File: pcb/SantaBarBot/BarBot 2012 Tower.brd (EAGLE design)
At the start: 53.3 x 73.4 mm, 49 parts, among them J1 AVR_SPI_PRG_62X3_LOCK, J2 POWER_JACKSLT, U1 ATMEGA328P, U2 L298_BRIDGE_DRIVER, U3 742G04DBVR, U5 LMV324IDR, U6 SN75HVD179D

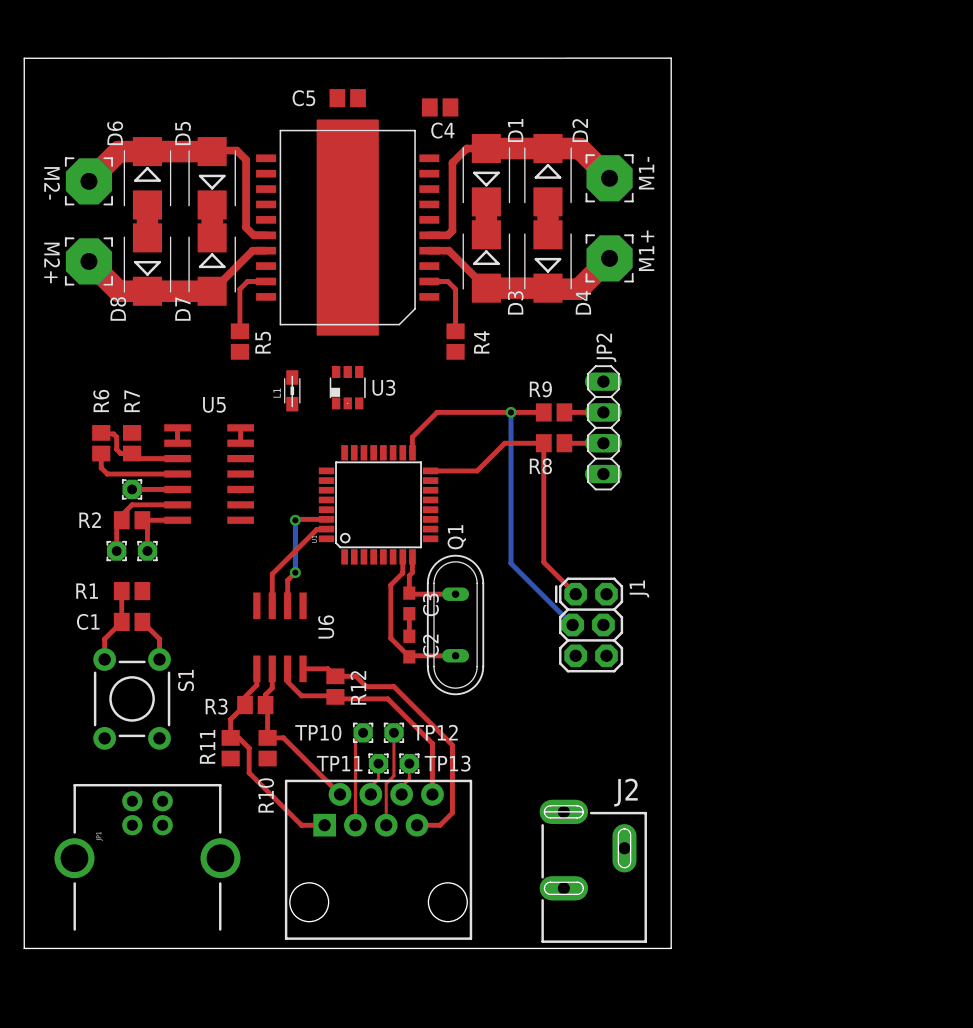
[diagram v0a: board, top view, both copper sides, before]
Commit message: Finished routing PCB, added PDFs of board and schematic to directory, generated netlist, pinlist, and partslist for design
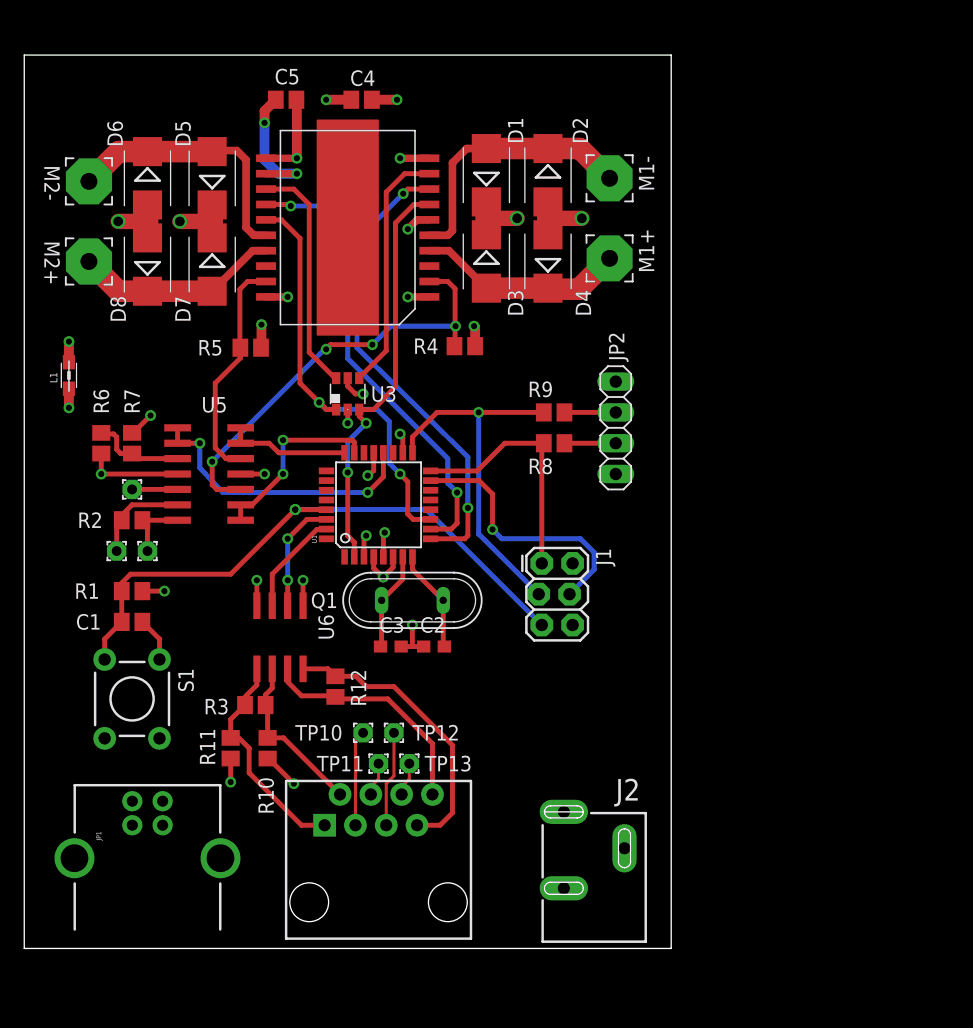
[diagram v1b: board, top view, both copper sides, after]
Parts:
- moved L1 18.5 mm to (3.68, 47.2)
- moved C4 6.51 mm to (27.8, 70.0)
- moved C5 5.08 mm to (21.6, 70.0)
- moved Q1 4.10 mm to (32.0, 28.7), turned to 0 degrees
- moved C3 3.87 mm to (30.2, 24.9), turned to 180 degrees
- moved J1 3.78 mm to (42.7, 31.8)
- moved C2 2.03 mm to (33.8, 24.9), turned to 0 degrees
- moved R5 1.02 mm to (18.7, 49.5), turned to 180 degrees
- moved JP2 1.02 mm to (48.8, 42.9)
- moved R4 0.85 mm to (36.3, 49.7), turned to 180 degrees
- moved U3 0.51 mm to (26.7, 45.7)
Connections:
- net !PD4/XCK/T0: now also U3.4; no longer U3.6
- net !PD7/AIN1: now also U3.6; no longer U3.4
- net PB6/XTAL1: now also C3.2, Q1.1; no longer C2.2, Q1.2
- net PB7/XTAL2: now also C2.2, Q1.2; no longer C3.2, Q1.1
- net PD4/XCK/T0: now also U3.3; no longer U3.1
- net PD7/AIN1: now also U3.1; no longer U3.3
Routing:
- net GND: track 13.2 -> 80.2 mm, vias 0 -> 13
- net +5V: track 0.00 -> 50.5 mm, vias 0 -> 10
- net PC6/!RESET: track 6.22 -> 50.6 mm, vias 0 -> 2
- net PD5/T1: track 0.00 -> 39.1 mm, vias 0 -> 2
- net PD6/AIN0: track 0.00 -> 37.6 mm, vias 0 -> 2
- net PD7/AIN1: track 0.00 -> 36.0 mm, vias 0 -> 2
- net PD4/XCK/T0: track 0.00 -> 33.9 mm, vias 0 -> 2
- net SENSE_A: track 5.89 -> 36.3 mm, vias 0 -> 4
- net AREF: track 1.27 -> 23.7 mm, vias 0 -> 2
- net PB3/MOSI/OC2: track 0.00 -> 21.9 mm, vias 0 -> 1
- net !PD4/XCK/T0: track 0.00 -> 20.4 mm
- net !PD7/AIN1: track 0.00 -> 19.4 mm
- net PC0/ADC0: track 0.00 -> 15.4 mm, vias 0 -> 2
- net SENSE_B: track 5.89 -> 18.8 mm
- net GNDA: track 5.42 -> 18.0 mm, vias 0 -> 6
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- added copper zone on layer 15, net +5V
- added copper zone on layer 15, net +5V/2
- added copper zone on layer 2, net GND
- added copper zone on layer 2, net GNDA
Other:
- board size 53.3 x 73.4 mm -> 53.3 x 73.7 mm

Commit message: Changed board to 2 layers, 3x3 inches.  Fully routed, DRC and ERC run, all errors corrected.  PDFs generated
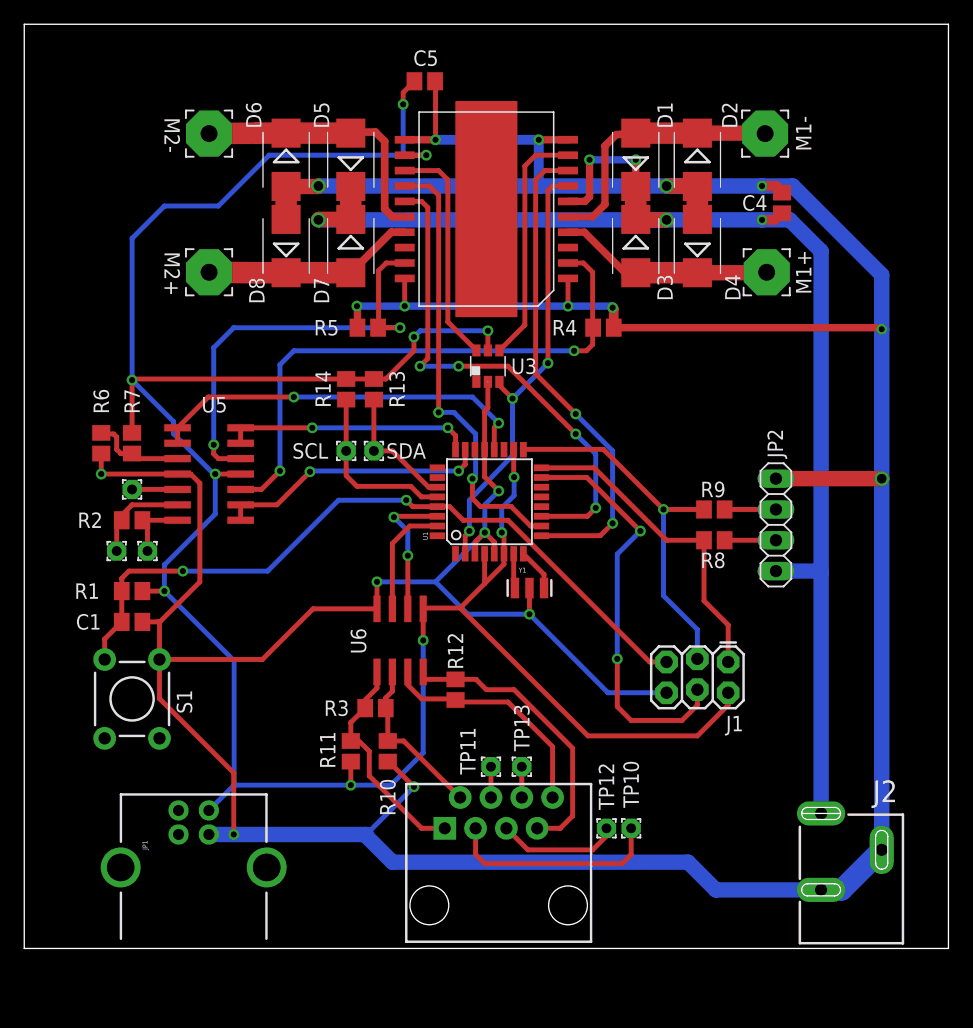
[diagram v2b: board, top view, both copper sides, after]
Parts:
- removed C2, C3: 22pF, rcl:C0603
- removed L1: (no value), wuerth-elektronik:0805
- removed Q1: (no value), special:QS
- added R13, R14: 0.1R, rcl:R2012
- added SCL, SDA: (no value), wirepad:1,6/0,8
- added Y1: 16MHz, SparkFun-FreqCtrl:RESONATOR-SMD
- moved C4 35.7 mm to (62.5, 61.5), turned to 270 degrees
- moved TP10 23.5 mm to (50.0, 9.91), turned to 270 degrees
- moved J2 21.2 mm to (63.1, -2.67)
- moved TP12 19.2 mm to (48.0, 9.91), turned to 90 degrees
- moved J1 17.4 mm to (58.0, 23.6), turned to 180 degrees
- moved JP2 15.4 mm to (62.0, 34.9)
- moved R8 15.4 mm to (56.9, 33.7)
- moved R9 15.4 mm to (56.9, 36.2)
- moved M1- 13.3 mm to (61.1, 67.2)
- moved M1+ 13.0 mm to (61.2, 55.8)
- moved D2 12.4 mm to (55.5, 65.0)
- moved D4 12.4 mm to (55.5, 57.9)
- moved D1 12.4 mm to (50.4, 65.0)
- moved D3 12.4 mm to (50.4, 57.9)
- moved U3 11.8 mm to (38.2, 48.0)
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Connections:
- removed net GNDA: C4.1, D2.A, D4.A, D6.A, D8.A, J2.GND@1, J2.GND@2, JP2.4, L1.2, R4.1, R5.1
- net +5V: now also R13.2, R14.2
- net GND: now also C4.1, D2.A, D4.A, D6.A, D8.A, J2.GND@1, J2.GND@2, JP2.4, R4.1, R5.1, Y1.2; no longer C2.1, C3.1, L1.1
- net PB6/XTAL1: now also Y1.1; no longer C3.2, Q1.1
- net PB7/XTAL2: now also Y1.3; no longer C2.2, Q1.2
- net PC4/ADC4/SDA: now also R13.1, SDA.1
- net PC5/ADC5/SCL: now also R14.1, SCL.1
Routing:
- net GND: track 80.2 -> 378.8 mm, vias 13 -> 18
- net +5V: track 50.5 -> 211.8 mm, vias 10 -> 11
- net +5V/2: track 14.8 -> 116.2 mm, vias 4 -> 5
- net GNDA: track 18.0 -> 0.00 mm, vias 6 -> 0
- net SENSE_B: track 18.8 -> 36.1 mm, vias 0 -> 2
- net PC5/ADC5/SCL: track 0.00 -> 14.5 mm
- net PB3/MOSI/OC2: track 21.9 -> 34.1 mm, vias 1 -> 2
- net SENSE_A: track 36.3 -> 47.5 mm, vias 4 -> 2
- net PC4/ADC4/SDA: track 0.00 -> 10.7 mm
- net PC1/ADC1: track 10.2 -> 20.4 mm, vias 0 -> 2
- net N$1: track 7.88 -> 17.8 mm
- net PC6/!RESET: track 50.6 -> 60.4 mm
- net AREF: track 23.7 -> 32.0 mm
- net PD7/AIN1: track 36.0 -> 43.5 mm, vias 2 -> 4
- net PC0/ADC0: track 15.4 -> 22.5 mm
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- removed copper zone on layer 15, net +5V
- removed copper zone on layer 15, net +5V/2
- removed copper zone on layer 2, net GND
- removed copper zone on layer 2, net GNDA
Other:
- board size 53.3 x 73.7 mm -> 76.2 x 76.2 mm

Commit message: Added 2nd RJ45 jack, added testpoints for UART, moved silk layer to copper.  Cleaned up a couple things in the schematic.  Removed some testpoints.
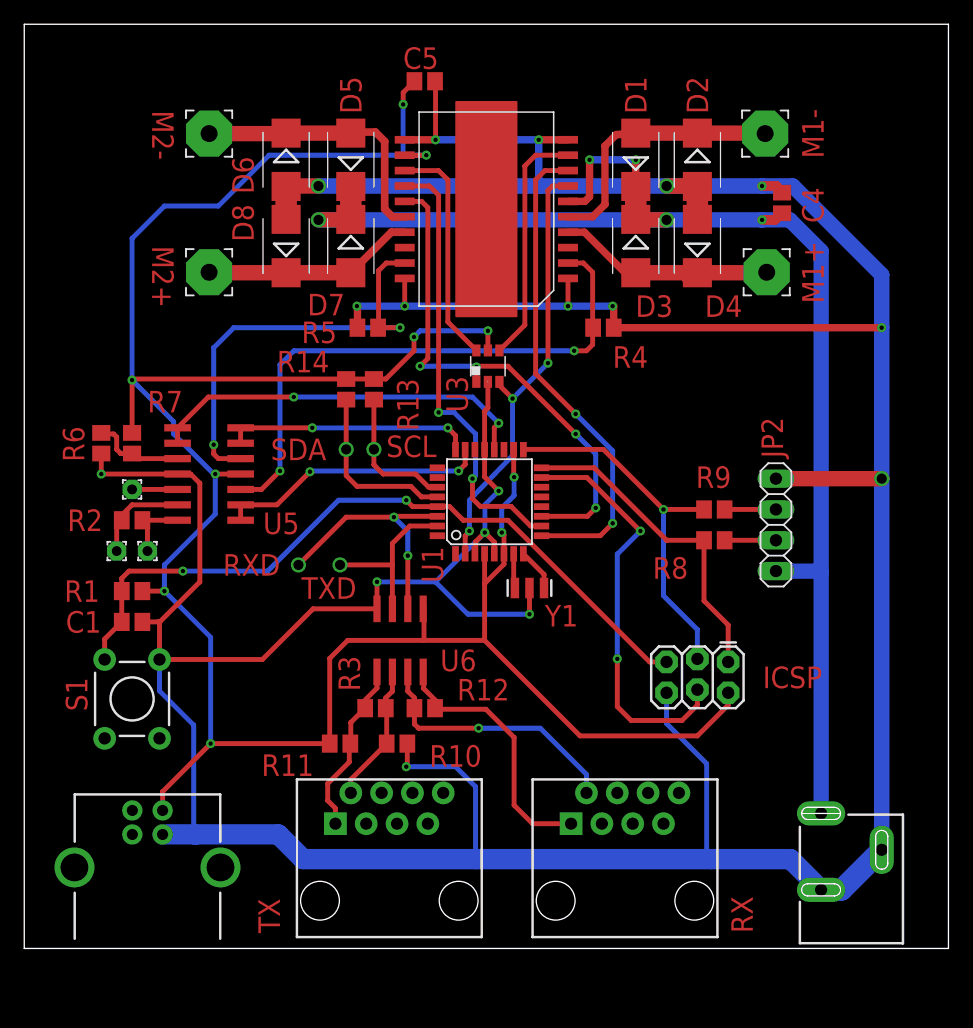
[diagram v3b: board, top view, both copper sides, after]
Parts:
- removed SCL, SDA, TP10, TP11, TP12, TP13: (no value), wirepad:1,6/0,8
- removed U$1: RJ45-8PTH, SparkFun-Connectors:RJ45-8
- added RX, TX: RJ45-8PTH, SparkFun-Connectors:RJ45-8
- R13, R14: value 0.1R -> 4.7k
- moved JP1 3.81 mm to (10.2, 9.40)
- moved R12 2.96 mm to (33.0, 19.8), turned to 0 degrees
- moved R11 1.09 mm to (26.0, 16.9), turned to 180 degrees
- moved R10 0.99 mm to (30.7, 16.9), turned to 180 degrees
- renumbered J1 to ICSP
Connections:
- removed net N$1: TP10.1, U$1.3
- removed net N$2: TP11.1, U$1.4
- removed net N$4: TP12.1, U$1.5
- removed net N$5: TP13.1, U$1.6
- new net RJ_RX_3: RX.3
- new net RJ_RX_4: RX.4
- new net RJ_RX_5: RX.5
- new net RJ_RX_6: RX.6
- new net RJ_RX_7: RX.7
- new net RJ_RX_8: RX.8
- new net RJ_TX_3: TX.3
- new net RJ_TX_4: TX.4
- new net RJ_TX_5: TX.5
- new net RJ_TX_6: TX.6
- new net RJ_TX_7: TX.7
- new net RJ_TX_8: TX.8
- net !RS485_RX: now also RX.2; no longer U$1.8
- net !RS485_TX: now also TX.2; no longer U$1.2
- net PC4/ADC4/SDA: no longer SDA.1
- net PC5/ADC5/SCL: no longer SCL.1
- net RS485_RX: now also RX.1; no longer U$1.7
- net RS485_TX: now also TX.1; no longer U$1.1
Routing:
- net N$1: track 17.8 -> 0.00 mm
- net N$4: track 10.1 -> 0.00 mm
- net GND: track 378.8 -> 388.4 mm, vias 18 -> 17
- net PD0/RXD: track 11.6 -> 21.1 mm, vias 2 -> 3
- net PD1/TXD: track 9.70 -> 14.0 mm, vias 0 -> 1
- net RS485_TX: track 18.5 -> 14.6 mm
- net !RS485_RX: track 19.3 -> 22.0 mm, vias 0 -> 1
- net N$5: track 2.54 -> 0.00 mm
- net N$2: track 2.54 -> 0.00 mm
- net RS485_RX: track 24.2 -> 22.0 mm
- net !RS485_TX: track 13.9 -> 11.8 mm
- net +5V: track 211.8 -> 209.9 mm, vias 11 -> 10
- net PC4/ADC4/SDA: track 10.7 -> 11.4 mm, vias 0 -> 1
- net PC5/ADC5/SCL: vias 0 -> 1
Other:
- board text added: "RX"
- board text added: "RXD"
- board text added: "SCL"
- board text added: "SDA"
- board text added: "TX"
- board text added: "TXD"

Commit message: Fixed component IDs so they don't violate clearance requirements, made them smaller.  Routed extra opamp to unused ADC pin.
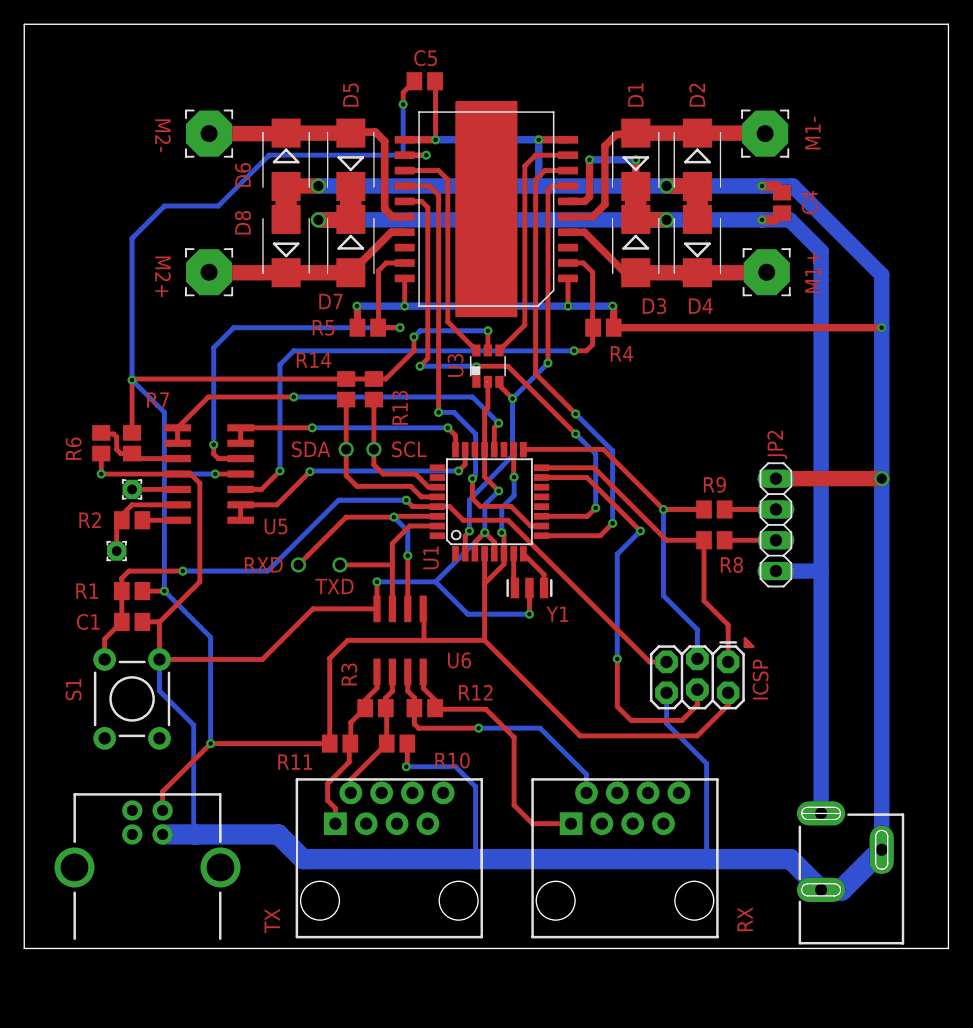
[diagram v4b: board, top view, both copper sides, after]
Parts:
- removed PAD3: (no value), wirepad:1,6/0,8
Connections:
- removed net N$7: PAD3.1, R2.1, U5.14
- net ADC6: now also R2.1, U5.14
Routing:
- net N$7: track 5.61 -> 0.00 mm
- net ADC6: track 0.00 -> 3.49 mm
- net N$1: track 0.00 -> 2.93 mm
- net +5V: track 209.9 -> 210.5 mm

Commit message: Board ready for review.  Rendered in 3D, see board_render.png.  Netlist/pinlist/partlist/pdfs updated
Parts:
- removed U6: SN75HVD179D, texas:SO-08
- added C2, C3: 100n, rcl:C0805
- added LED1, LED2, LED3: (no value), led:CHIPLED_0805
- added R15, R16, R17: 0.1R, rcl:R0805
- added U4: LMV324IDR, bb_parts_OpAmp:SO14
- C1, C5: device rcl:C2012 -> rcl:C0805
- C4: value 100n -> (none); device rcl:C2012 -> rcl:E3,5-8
- JP1: device SparkFun-Connectors:USB-B-PTH -> con-berg:PN61729-S
- M1+, M1-, M2+, M2-: device wirepad:3,81/1,4 -> wirepad:3,81/1,1
- R1, R10, R11, R12, R13, R14, R2, R4, R6, R8: device rcl:R2012 -> rcl:R0805
- R3: value 120 -> 0.1R; device rcl:R2012 -> rcl:R0805
- R5: value 0.1R -> (none); device rcl:R2012 -> rcl:R0805
- R7: value (none) -> 4.7k; device rcl:R2012 -> rcl:R0805
- R9: value 4.7k -> 120; device rcl:R2012 -> rcl:R0805
- U2: value L298_BRIDGE_DRIVER -> SN75HVD179D; device SparkFun-PowerIC:POWERSO20 -> texas:SO-08
- U5: value LMV324IDR -> L298; device bb_parts_OpAmp:SO14 -> st-microelectronics:MULTIWATT-15
- moved C5 62.0 mm to (10.5, 13.7), turned to 0 degrees
- moved R7 48.7 mm to (56.9, 33.7), turned to 0 degrees
- moved C4 43.9 mm to (68.1, 17.9), turned to 0 degrees
- moved R3 40.3 mm to (48.8, 54.9)
- moved U2 36.3 mm to (31.0, 25.4)
- moved R9 32.4 mm to (29.0, 19.8), turned to 180 degrees
- moved U5 29.6 mm to (38.4, 57.5), turned to 180 degrees
- moved R5 23.9 mm to (6.35, 41.7), turned to 90 degrees
- moved R4 20.4 mm to (27.7, 54.9), turned to 0 degrees
- moved D5 4.38 mm to (23.1, 67.2)
- moved D6 4.38 mm to (17.8, 67.2)
- moved M2+ 4.38 mm to (11.4, 57.9)
- moved D7 4.38 mm to (23.1, 60.1)
- moved D8 4.38 mm to (17.8, 60.1)
- moved M2- 4.38 mm to (11.4, 69.3)
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- renumbered JP2 to LED
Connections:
- new net N$2: LED1.A, R15.1
- new net N$4: LED2.A, R16.1
- new net N$5: LED3.A, R17.1
- net !PD4/XCK/T0: now also U5.7; no longer U2.9
- net !PD7/AIN1: now also U5.12; no longer U2.13
- net !RS485_RX: now also U2.7; no longer U6.7
- net !RS485_TX: now also R9.1, U2.6; no longer R3.1, U6.6
- net +5V: now also C2.2, JP1.2, R15.2, R16.2, R17.2, R6.2, U2.1, U4.4; no longer JP1.VBUS, R7.2, U2.12, U6.1
- net +5V/2: now also C3.2, C4.+, U5.9; no longer C4.2, U2.6
- net ADC6: now also U4.14; no longer U5.14
- net AREF: now also U4.8, U4.9; no longer U5.8, U5.9
- net GND: now also C2.1, C3.1, C4.-, JP1.3, R3.1, U2.4, U4.11, U5.8; no longer C4.1, JP1.GND, R6.1, U2.1, U2.10, U2.11, U2.20, U5.11, U6.4
- net M1+: now also U5.2; no longer U2.4
- net M1-: now also U5.3; no longer U2.5
- net M2+: now also U5.14; no longer U2.17
- net M2-: now also U5.13; no longer U2.16
- net N$10: now also R5.2, R6.1, U4.10; no longer R6.2, R7.1, U5.10
- net N$3: now also U4.13; no longer U5.13
- net PB0/ICP: now also LED1.C
- net PB1/OC1A: now also LED2.C
- net PB2/SS/OC1B: now also LED3.C
- net PB4/MISO: now also R7.1; no longer R8.1
- net PB5/SCK: now also R8.1; no longer R9.1
- net PC0/ADC0: now also U4.1, U4.2; no longer U5.1, U5.2
- net PC1/ADC1: now also U4.6, U4.7; no longer U5.6, U5.7
- net PD0/RXD: now also U2.2; no longer U6.2
- net PD1/TXD: now also U2.3; no longer U6.3
- net PD4/XCK/T0: now also U5.5; no longer U2.7
- net PD5/T1: now also U5.6; no longer U2.8
- net PD6/AIN0: now also U5.11; no longer U2.14
- net PD7/AIN1: now also U5.10; no longer U2.15
- net RS485_RX: now also U2.8; no longer U6.8
- net RS485_TX: now also R9.2, U2.5; no longer R3.2, U6.5
- net SENSE_A: now also R3.2, U4.3, U5.1; no longer R4.2, U2.2, U5.3
- net SENSE_B: now also R4.2, U4.5, U5.15; no longer R5.2, U2.19, U5.5
- net SPI_MISO: now also R7.2; no longer R8.2
- net SPI_SCK: now also R8.2; no longer R9.2
- net TP1: now also U4.12; no longer U5.12
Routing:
- net ADC6: track 3.49 -> 35.8 mm, vias 0 -> 2
- net +5V: track 210.5 -> 193.7 mm, vias 10 -> 9
- net PB2/SS/OC1B: track 0.00 -> 12.6 mm
- net PB1/OC1A: track 0.00 -> 10.7 mm
- net PD5/T1: track 40.2 -> 30.0 mm
- net PB0/ICP: track 0.00 -> 8.78 mm
- net SENSE_A: track 47.5 -> 55.6 mm
- net PD4/XCK/T0: track 36.4 -> 44.4 mm
- net PB3/MOSI/OC2: track 34.1 -> 26.1 mm, vias 2 -> 0
- net !PD7/AIN1: track 18.9 -> 12.4 mm
- net GND: track 388.4 -> 382.7 mm, vias 17 -> 11
- net !PD4/XCK/T0: track 20.0 -> 16.0 mm
- net ADC7: track 0.00 -> 3.57 mm, vias 0 -> 1
- net PC3/ADC3: track 0.00 -> 3.53 mm, vias 0 -> 1
- net RS485_RX: track 22.0 -> 25.1 mm
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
